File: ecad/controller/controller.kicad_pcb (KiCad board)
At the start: 2 copper layers, 48.8 x 30.2 mm, 40 parts, among them J2 USB_C_Receptacle_PowerOnly_6P, SW1 RST, SW2 BOOT, SW3 USER1, U1 ESP32-S3-WROOM-1, U2 AMS1117-3.3, U3 SN74LVC1T45DBV, U4 USBLC6-2SC6

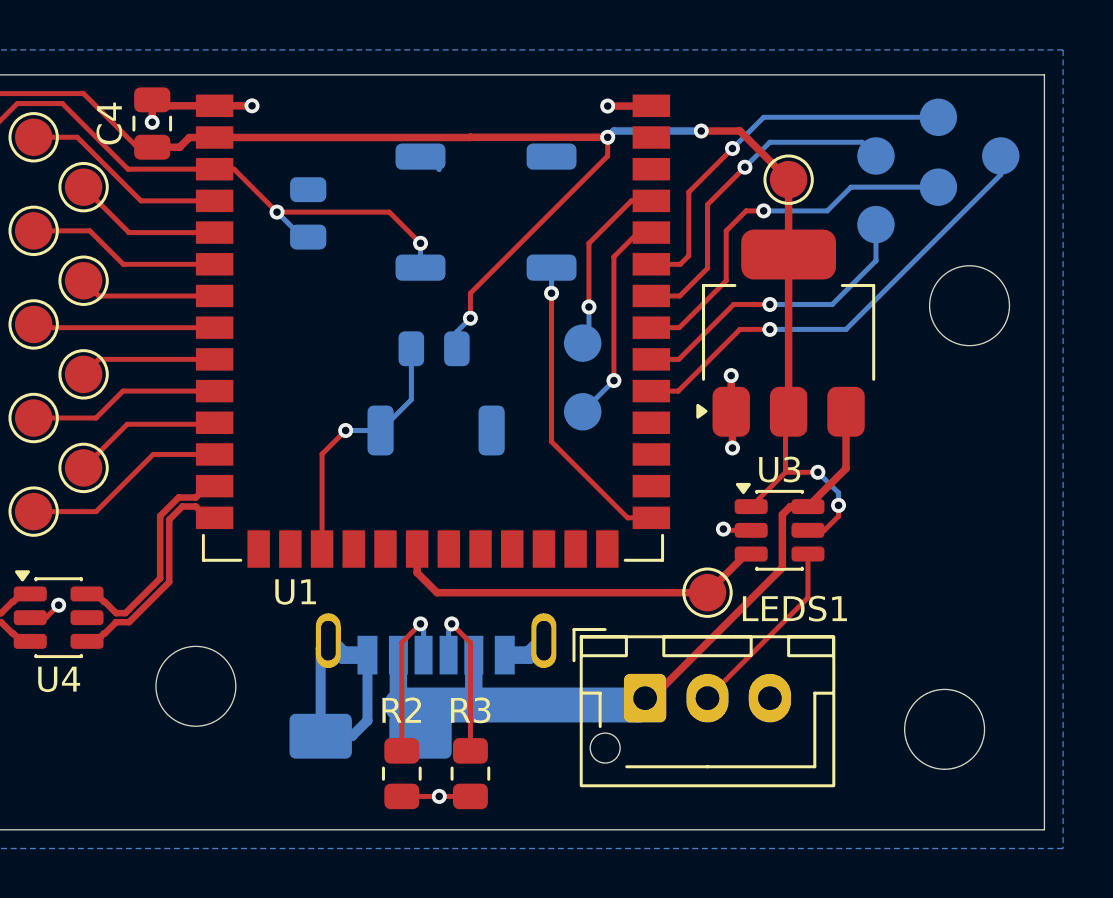
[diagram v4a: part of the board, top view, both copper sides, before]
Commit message: add decoupling caps; correct hole shape in usb-c footprint
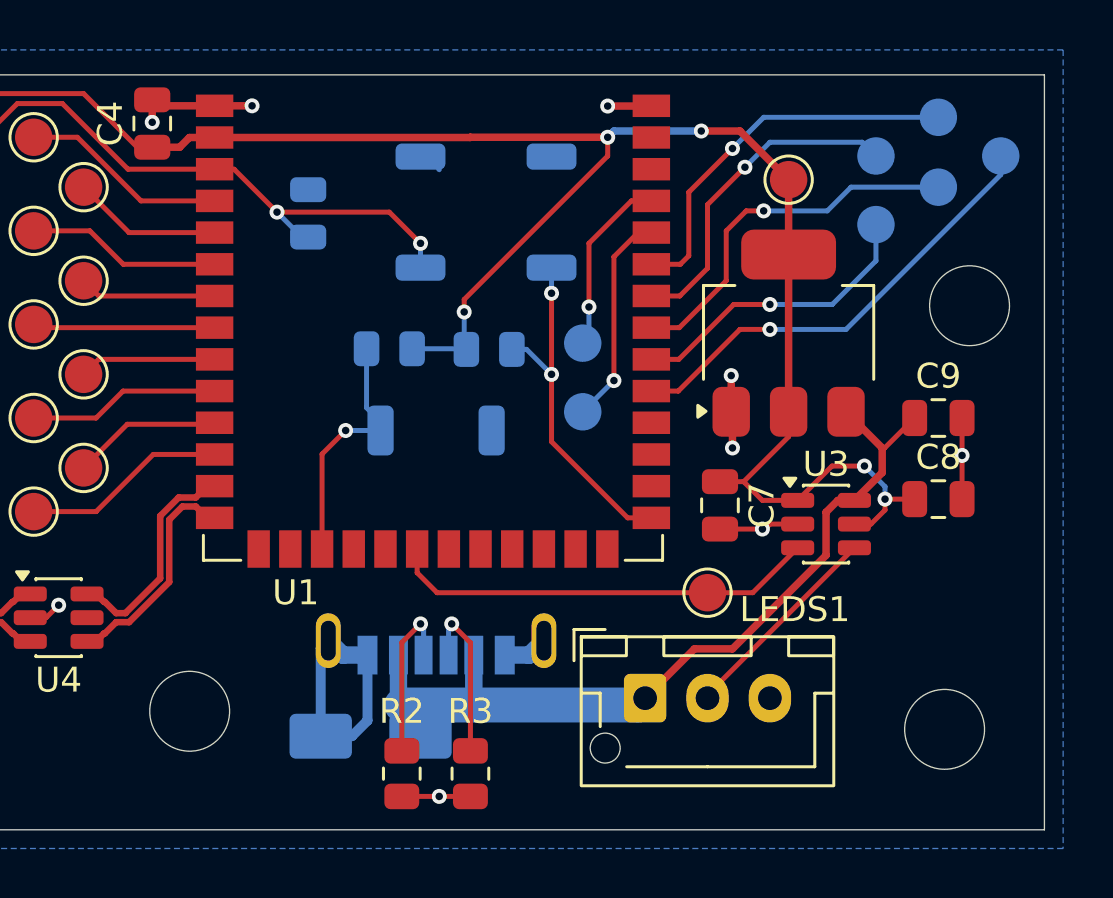
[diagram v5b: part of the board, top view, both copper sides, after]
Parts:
- added C7: 0.1uF, Capacitor_SMD:C_0805_2012Metric, F.Cu at (85.2, 52.0)
- added C8: 10uF, Capacitor_SMD:C_0805_2012Metric, F.Cu at (94.0, 51.8)
- added C9: 10uF, Capacitor_SMD:C_0805_2012Metric, F.Cu at (94.0, 48.5)
- added R5: 10kΩ, Resistor_SMD:R_0805_2012Metric, B.Cu at (76.0, 45.8)
- moved U3 1.88 mm to (89.5, 52.8)
- moved R4 1.80 mm to (72.0, 45.7)
- moved H2 1.03 mm to (64.0, 60.2)
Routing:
- net +3V3: track 71.0 -> 79.0 mm
- net GND: track 29.5 -> 34.9 mm, vias 10 -> 11
- net +5V: track 30.0 -> 33.8 mm
- net /IO0: track 12.2 -> 14.2 mm, vias 1 -> 2
- net /LED_GPIO: track 15.3 -> 17.3 mm
- net /LED_SIG: track 7.84 -> 8.46 mm

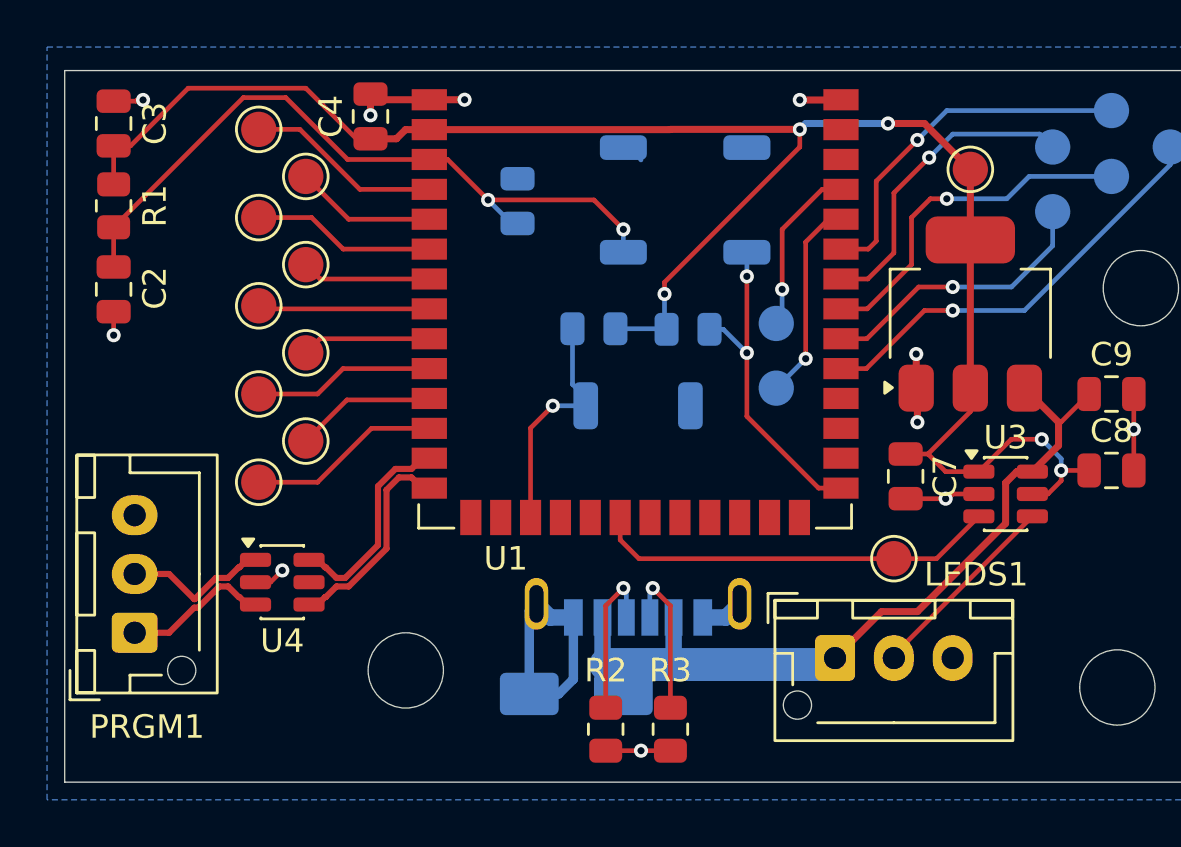
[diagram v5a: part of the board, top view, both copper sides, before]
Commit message: model and link USB-C 3D connector
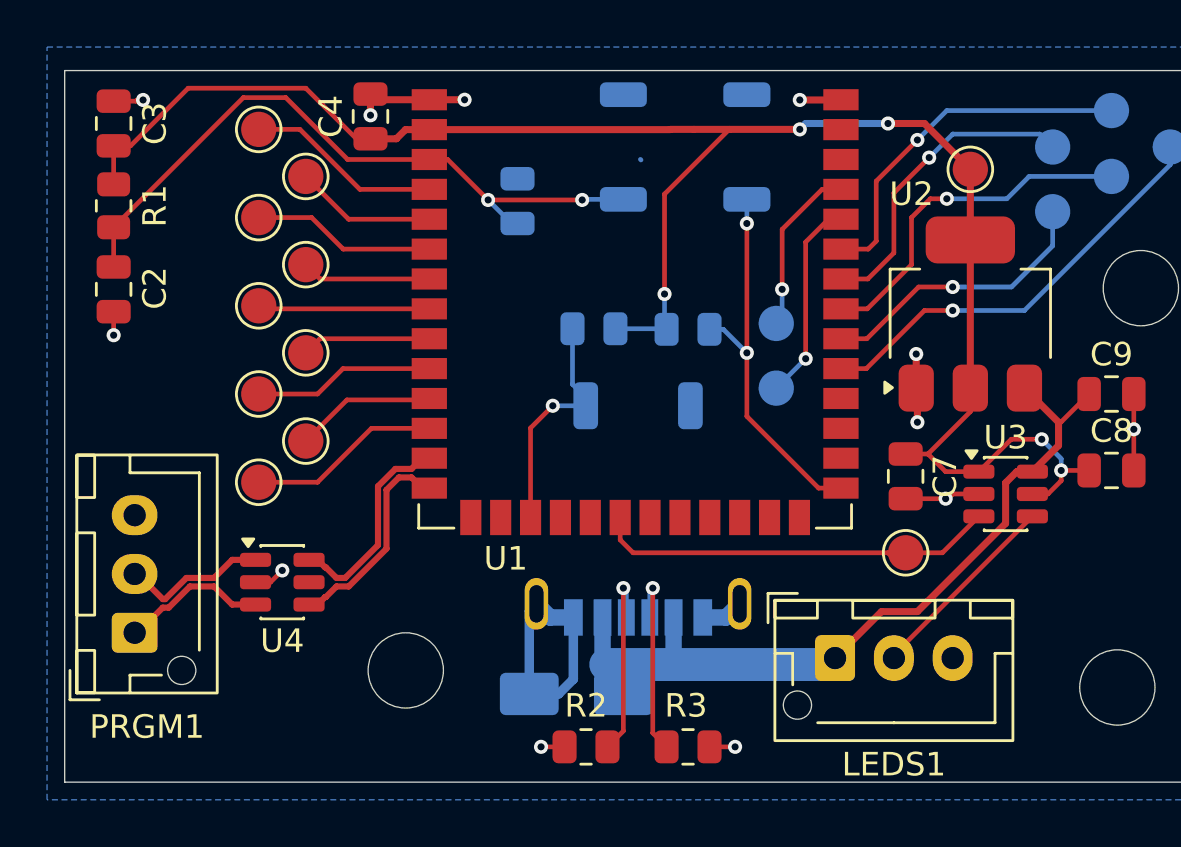
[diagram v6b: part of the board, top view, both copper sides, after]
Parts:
- SW1: value RST -> SW
- SW2: value BOOT -> SW
- SW3: value USER1 -> SW
- moved SW1 2.25 mm to (73.2, 38.0)
- moved SW2 2.25 mm to (78.5, 38.0)
- moved R2 1.12 mm to (71.7, 63.5), turned to 180 degrees
- moved R3 1.06 mm to (76.0, 63.5), turned to 0 degrees
- moved LED_TP1 0.56 mm to (85.2, 55.2)
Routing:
- net /IO0: track 14.2 -> 16.5 mm
- net Net-(J2-CC2): track 6.70 -> 8.33 mm
- net Net-(J2-CC1): track 6.70 -> 8.30 mm
- net /EN: track 30.9 -> 29.5 mm
- net +3V3: track 79.0 -> 77.8 mm
- net GND: track 34.9 -> 34.2 mm, vias 11 -> 12

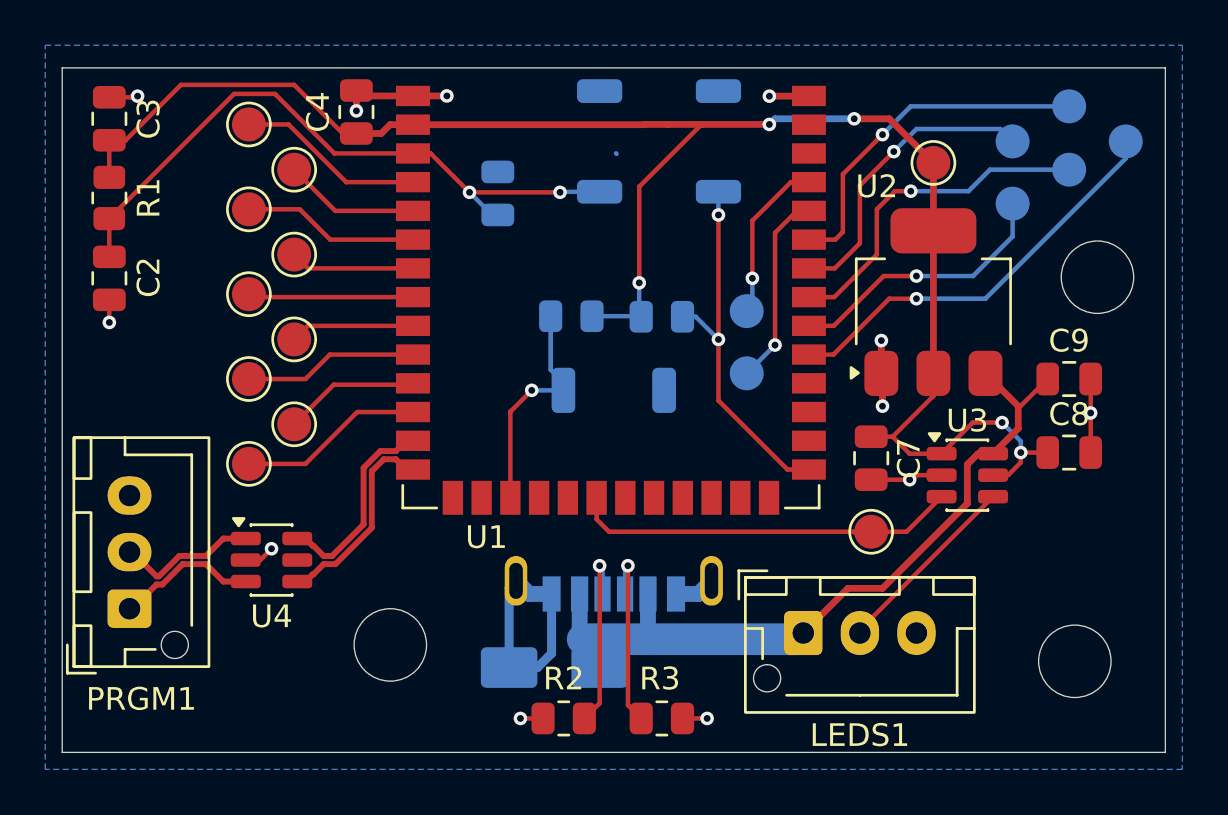
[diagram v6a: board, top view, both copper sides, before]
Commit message: final design review for v1 order; reroute some components; add LED to controller
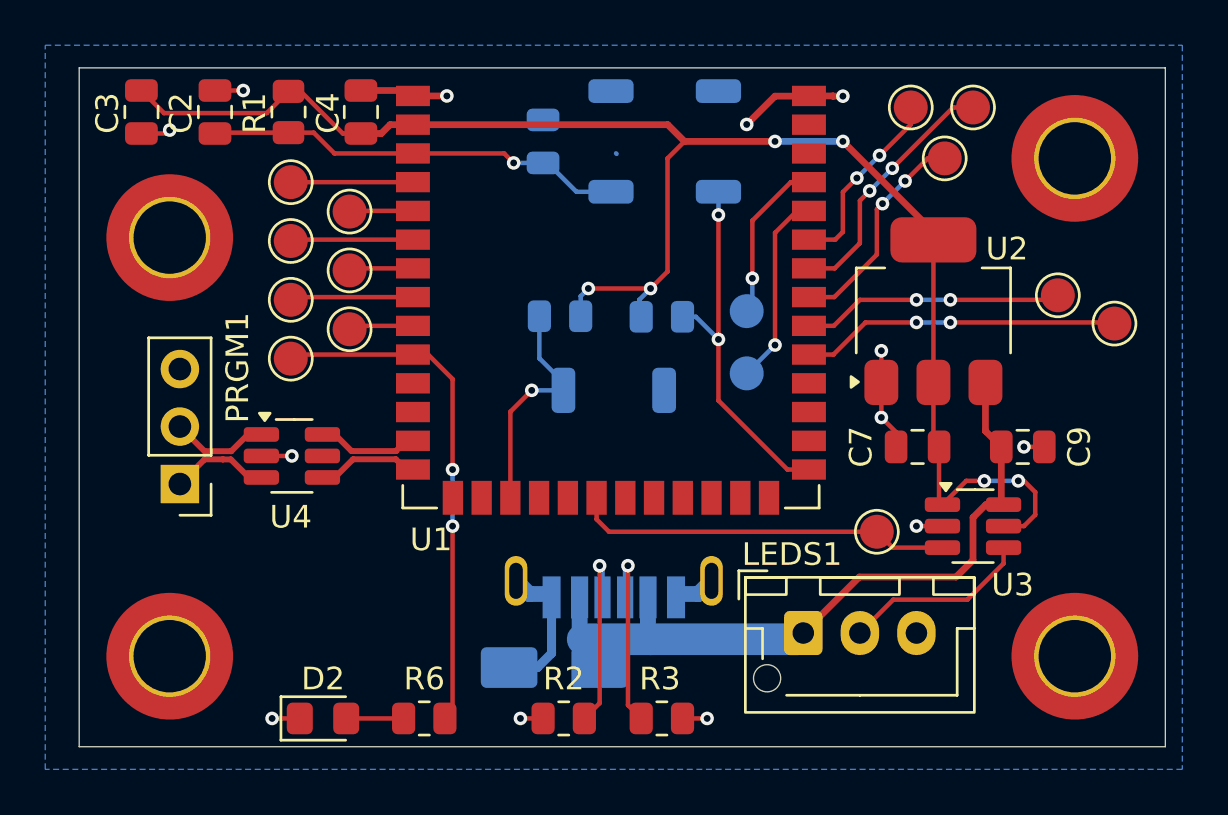
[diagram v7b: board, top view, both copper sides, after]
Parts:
- removed 3V3, IO18, IO8: TestPoint, TestPoint:TestPoint_Pad_D1.5mm
- removed C8: 10uF, Capacitor_SMD:C_0805_2012Metric
- added D2: LED, LED_SMD:LED_0805_2012Metric_Pad1.15x1.40mm_HandSolder, F.Cu at (61.0, 63.5)
- added H4: MountingHole, MountingHole:MountingHole_3.2mm_M3_DIN965_Pad_TopOnly, F.Cu at (54.2, 42.2)
- added R6: 50Ω, Resistor_SMD:R_0805_2012Metric, F.Cu at (65.5, 63.5)
- H1, H2, H3: footprint MountingHole:MountingHole_3.2mm_M3 -> MountingHole:MountingHole_3.2mm_M3_DIN965_Pad_TopOnly
- IO38, IO39, IO40, IO41, IO42: moved to F.Cu
- PRGM1: footprint Connector_JST:JST_XH_B3B-XH-AM_1x03_P2.50mm_Vertical -> Connector_PinHeader_2.54mm:PinHeader_1x03_P2.54mm_Vertical
- U3, U4: footprint Package_TO_SOT_SMD:SOT-23-6 -> Package_TO_SOT_SMD:SOT-23-6_Handsoldering
- moved H2 9.76 mm to (54.2, 60.8)
- moved R1 8.78 mm to (59.5, 36.7)
- moved C2 8.71 mm to (56.2, 36.7), turned to 90 degrees
- moved IO38 8.07 mm to (96.0, 46.0), turned to 0 degrees
- moved IO42 7.00 mm to (87.0, 36.5), turned to 0 degrees
- moved PRGM1 5.94 mm to (54.7, 53.1), turned to 180 degrees
- moved IO40 5.52 mm to (88.5, 38.8), turned to 0 degrees
- moved H1 5.34 mm to (94.2, 38.8)
- moved U4 4.69 mm to (59.6, 51.9)
- moved IO39 4.52 mm to (93.5, 44.8), turned to 0 degrees
- moved C9 3.63 mm to (92.0, 51.5)
- moved IO4 3.15 mm to (59.6, 39.8)
- moved IO5 3.07 mm to (62.2, 41.1)
- moved C5 3.05 mm to (70.8, 38.0)
- moved IO7 2.55 mm to (62.2, 43.7)
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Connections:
- U1 pad 11: Net-(U1-IO18) -> unconnected-(U1-IO18-Pad11)
- U1 pad 12: Net-(U1-IO8) -> unconnected-(U1-IO8-Pad12)
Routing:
- net Net-(U1-IO17): track 8.20 -> 22.8 mm, vias 0 -> 2
- net /EN: track 29.5 -> 18.6 mm, vias 2 -> 1
- net Net-(U1-IO8): track 8.20 -> 0.00 mm
- net Net-(U1-IO42): track 15.4 -> 8.39 mm, vias 1 -> 2
- net +3V3: track 77.8 -> 71.0 mm, vias 5 -> 6
- net Net-(U1-IO18): track 6.00 -> 0.00 mm
- net Net-(U1-IO40): track 15.0 -> 9.71 mm, vias 1 -> 2
- net /USB_D-: track 9.00 -> 4.49 mm
- net /USB_D+: track 9.00 -> 4.52 mm
- net Net-(U1-IO38): track 18.3 -> 14.0 mm, vias 1 -> 2
- net Net-(U1-IO4): track 8.81 -> 5.40 mm
- net Net-(U1-IO5): track 6.00 -> 2.81 mm
- net GND: track 34.2 -> 31.0 mm, vias 12 -> 13
- net Net-(U1-IO6): track 8.31 -> 5.42 mm
- net Net-(U1-IO7): track 5.50 -> 2.84 mm
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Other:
- board size 48.8 x 30.2 mm -> 48 x 30 mm
